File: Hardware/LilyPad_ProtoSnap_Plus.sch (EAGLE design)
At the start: 141 parts, among them J1 SEWTAP_LONG-2SIDE, J10 SEWTAP_LONG-2SIDE, J11 SEWTAP_LONG-2SIDE, J12 SEWTAP_LONG-2SIDE, J13 SEWTAP_LONG-2SIDE, J14 SEWTAP_LONG-2SIDE, J15 AMP FCI 10103594-0001LF, J2 SEWTAP_LONG-2SIDE, J3 SEWTAP_LONG-2SIDE, J4 SEWTAP_LONG-2SIDE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

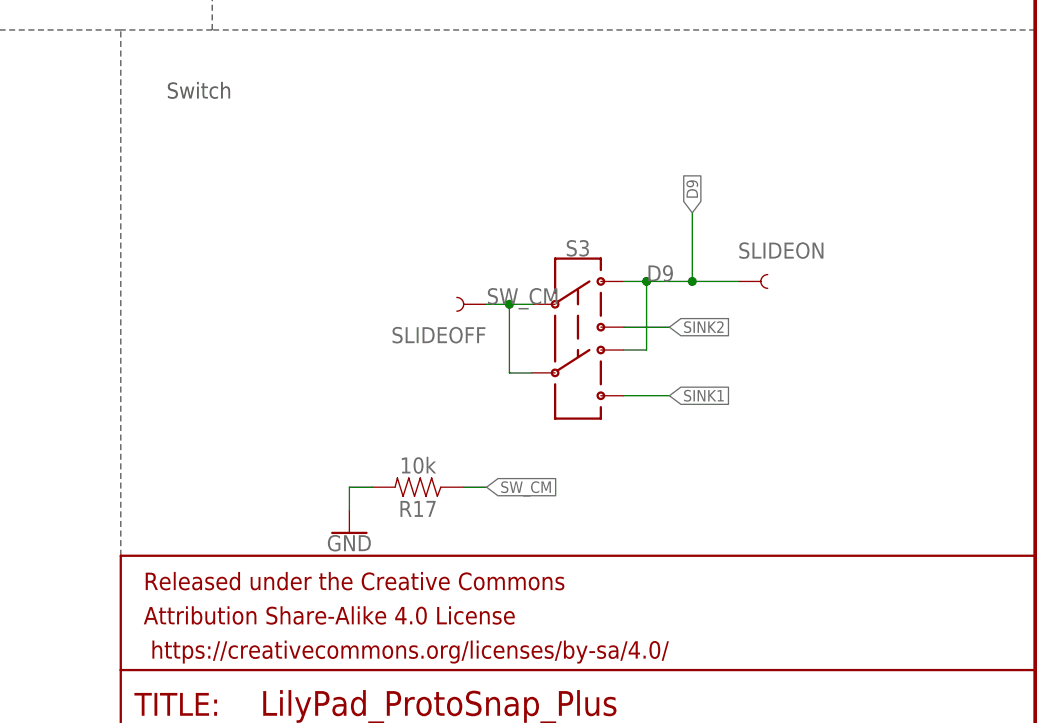
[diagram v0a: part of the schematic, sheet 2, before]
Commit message: Added changes from reds review
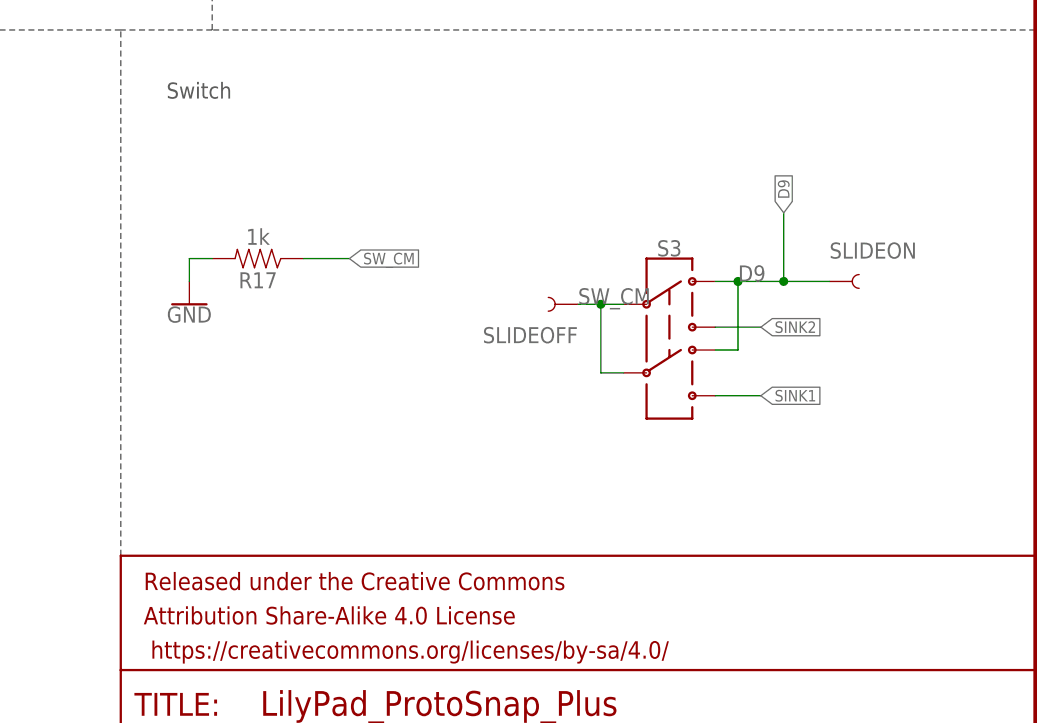
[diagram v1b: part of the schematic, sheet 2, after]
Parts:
- LED3: PROD_ID DIO-00819 -> (none)
- R17: value 10k -> 1k; device SparkFun-Resistors:10KOHM-0603-1/10W-1% -> SparkFun-Resistors:1KOHM-0603-1/10W-1%
- R6: value 330 -> 2.2k; device SparkFun-Resistors:330OHM-0603-1/10W-1% -> SparkFun-Resistors:2.2KOHM-0603-1/10W-1%; PROD_ID RES-00818 -> (none)
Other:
- note added: "Charge current factory set to 100mA I_CHG = 1000/R2"
- moved on the sheet: LED8, R17, R4, R5, S3, SLIDEOFF, SLIDEON

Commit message: Ran engineering checklist
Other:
- note added: "Supply 5.0V from USB, or 3.3-4.2V on battery connector."
- note removed: "v03"
- moved on the sheet: J16
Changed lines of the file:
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@@
 <setting verticaltext="up"/>
 </settings>
-<grid distance="0.1" unitdist="inch" unit="inch" style="lines" multiple="1" display="no" altdistance="0.05" altunitdist="inch" altunit="inch"/>
+<grid distance="0.1" unitdist="inch" unit="inch" style="lines" multiple="1" display="no" altdistance="0.01" altunitdist="inch" altunit="inch"/>
 <layers>
 <layer number="1" name="Top" color="4" fill="1" visible="no" active="no"/>
@@
 <text x="83.82" y="68.58" size="2.032" layer="97" font="vector">Charge current factory set to 100mA
 I_CHG = 1000/R2</text>
+<text x="5.08" y="5.08" size="2.032" layer="97" font="vector">Supply 5.0V from USB, or
+3.3-4.2V on battery connector.</text>
 </plain>
 <instances>
@@
 <attribute name="PROD_ID" x="139.7" y="93.98" size="1.27" layer="96" rot="R180" display="off"/>
 </instance>
-<instance part="LED2" gate="G$1" x="147.32" y="99.06" rot="R270">
+<instance part="LED2" gate="G$1" x="147.32" y="99.06" smashed="yes" rot="R270">
 <attribute name="PROD_ID" x="147.32" y="99.06" size="1.27" layer="96" rot="R270" display="off"/>
-</instance>
-<instance part="LED3" gate="G$1" x="154.94" y="93.98" rot="R270">
+<attribute name="NAME" x="142.748" y="105.791" size="1.778" layer="95" font="vector"/>
+<attribute name="VALUE" x="142.748" y="104.775" size="1.778" layer="96" font="vector" align="top-left"/>
+</instance>
+<instance part="LED3" gate="G$1" x="154.94" y="93.98" smashed="yes" rot="R270">
 <attribute name="PROD_ID" x="154.94" y="93.98" size="1.27" layer="96" rot="R270" display="off"/>
+<attribute name="NAME" x="150.368" y="89.789" size="1.778" layer="95" font="vector"/>
+<attribute name="VALUE" x="150.368" y="88.773" size="1.778" layer="96" font="vector" align="top-left"/>
 </instance>
 <instance part="LED4" gate="G$1" x="144.78" y="116.84" smashed="yes" rot="R90">
@@
 <attribute name="PROD_ID" x="101.6" y="45.72" size="1.778" layer="96" display="off"/>
 </instance>
-<instance part="GND11" gate="1" x="27.94" y="10.16"/>
-<instance part="U$4" gate="G$1" x="27.94" y="20.32"/>
+<instance part="GND11" gate="1" x="27.94" y="17.78"/>
+<instance part="U$4" gate="G$1" x="27.94" y="27.94"/>
 <instance part="GND12" gate="1" x="165.1" y="109.22"/>
 <instance part="U5" gate="G1" x="63.5" y="124.46"/>
@@
 <attribute name="NAME" x="33.02" y="43.18" size="1.778" layer="95" font="vector" rot="R180"/>
 </instance>
-<instance part="J16" gate="G$1" x="20.32" y="15.24" rot="R90"/>
+<instance part="J16" gate="G$1" x="20.32" y="22.86" rot="R90"/>
 <instance part="GND10" gate="1" x="10.16" y="106.68"/>
 <instance part="SUPPLY1" gate="G$2" x="109.22" y="50.8"/>
@@
 </segment>
 <segment>
-<wire x1="25.4" y1="17.78" x2="27.94" y2="17.78" width="0.1524" layer="91"/>
-<wire x1="27.94" y1="17.78" x2="27.94" y2="20.32" width="0.1524" layer="91"/>
+<wire x1="25.4" y1="25.4" x2="27.94" y2="25.4" width="0.1524" layer="91"/>
+<wire x1="27.94" y1="25.4" x2="27.94" y2="27.94" width="0.1524" layer="91"/>
 <pinref part="U$4" gate="G$1" pin="V_BATT"/>
 <pinref part="J16" gate="G$1" pin="+"/>
@@
 <segment>
 <pinref part="GND11" gate="1" pin="GND"/>
-<wire x1="25.4" y1="15.24" x2="27.94" y2="15.24" width="0.1524" layer="91"/>
-<wire x1="27.94" y1="15.24" x2="27.94" y2="12.7" width="0.1524" layer="91"/>
+<wire x1="25.4" y1="22.86" x2="27.94" y2="22.86" width="0.1524" layer="91"/>
+<wire x1="27.94" y1="22.86" x2="27.94" y2="20.32" width="0.1524" layer="91"/>
 <pinref part="J16" gate="G$1" pin="-"/>
 </segment>
@@
 <text x="53.34" y="86.36" size="1.778" layer="97">Buzzer</text>
 <text x="171.45" y="11.43" size="2.54" layer="94">Marshall Taylor</text>
-<text x="238.252" y="7.112" size="2.54" layer="94">v03</text>
+<text x="238.252" y="7.112" size="2.54" layer="94">v10</text>
 <text x="60.96" y="25.4" size="1.778" layer="97">Un-used
 sew taps</text>

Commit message: Updated reds QC check
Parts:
- D10: device newLilypadParts:SUNLEDSMD1 -> SparkFun-LED:SUNLEDSMD1
- U5: value ATMEGA32U4_NOARDQFN3 -> 32U4; device newLilypadParts:ATMEGA32U4_NOARDQFN3 -> SparkFun-IC-Microcontroller:ATMEGA32U4_NOARDQFN3
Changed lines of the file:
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@@
 <part name="U$4" library="SparkFun-PowerSymbols" deviceset="V_BATT" device=""/>
 <part name="GND12" library="SparkFun-PowerSymbols" deviceset="GND" device=""/>
-<part name="U5" library="newLilypadParts" deviceset="ATMEGA32U4_NOARD" device="QFN3" value="ATMEGA32U4_NOARDQFN3"/>
+<part name="U5" library="SparkFun-IC-Microcontroller" deviceset="ATMEGA32U4_NOARD" device="QFN3" value="32U4"/>
 <part name="J1" library="LilyPad-Wearables" deviceset="SEWTAP" device="_LONG-2SIDE" value="SEWTAP_LONG-2SIDE"/>
 <part name="J2" library="LilyPad-Wearables" deviceset="SEWTAP" device="_LONG-2SIDE" value="SEWTAP_LONG-2SIDE"/>
@@
 <part name="LOGO5" library="SparkFun-Aesthetics" deviceset="OSHW-LOGO" device="S"/>
 <part name="LOGO6" library="SparkFun-Aesthetics" deviceset="OSHW-LOGO" device="S"/>
-<part name="D10" library="newLilypadParts" deviceset="SUNLED" device="SMD1" value="XZM2CRKM2DGFBB45SCCB"/>
+<part name="D10" library="SparkFun-LED" deviceset="SUNLED" device="SMD1" value="XZM2CRKM2DGFBB45SCCB"/>
 <part name="TP5" library="SparkFun-Connectors" deviceset="TEST-POINT" device="3"/>
 <part name="TP6" library="SparkFun-Connectors" deviceset="TEST-POINT" device="3"/>

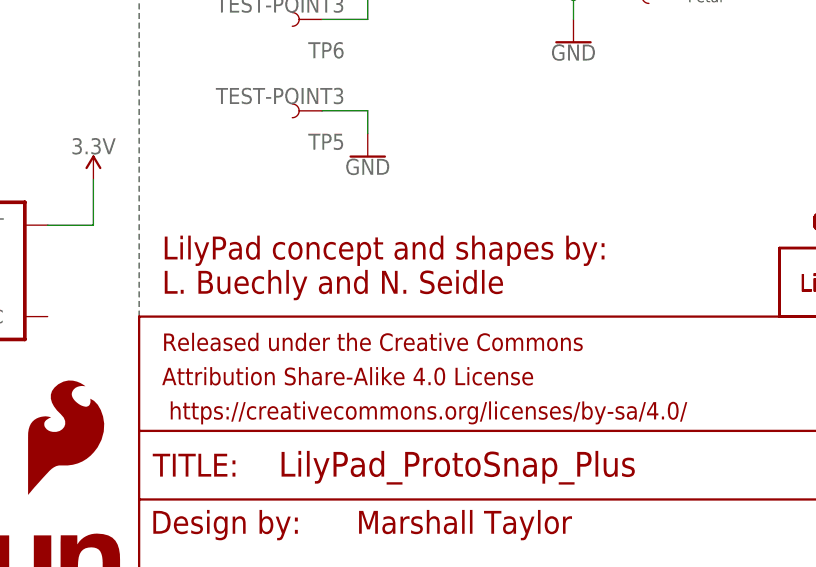
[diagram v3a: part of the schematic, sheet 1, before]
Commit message: Fixed spelling error
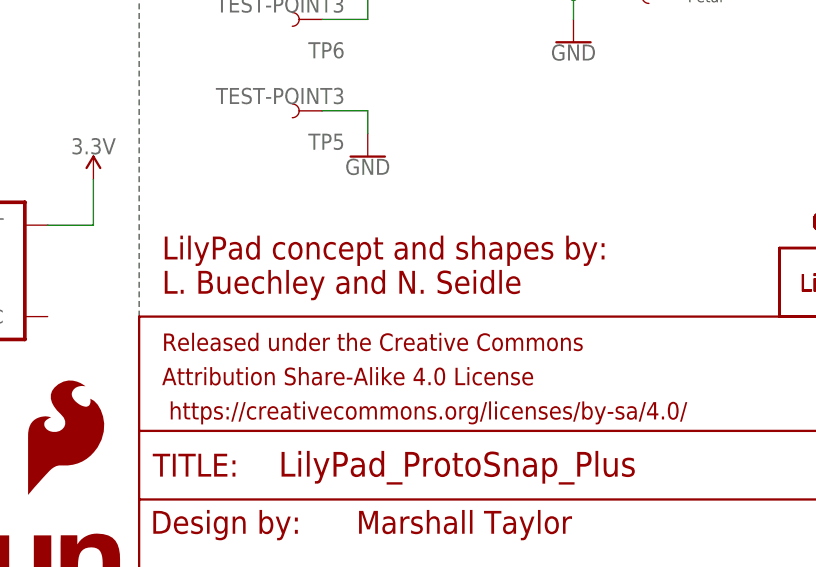
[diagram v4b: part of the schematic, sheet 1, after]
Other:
- note added: "LilyPad concept and shapes by: L. Buechley and N. Seidle"
- note removed: "LilyPad concept and shapes by: L. Buechly and N. Seidle"
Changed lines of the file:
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@@
 <text x="238.252" y="7.112" size="2.54" layer="94">v10</text>
 <text x="149.86" y="38.1" size="2.54" layer="94">LilyPad concept and shapes by:
-L. Buechly and N. Seidle</text>
+L. Buechley and N. Seidle</text>
 <wire x1="223.52" y1="182.88" x2="246.38" y2="182.88" width="0.1524" layer="97" style="shortdash"/>
 <wire x1="246.38" y1="182.88" x2="246.38" y2="154.94" width="0.1524" layer="97" style="shortdash"/>

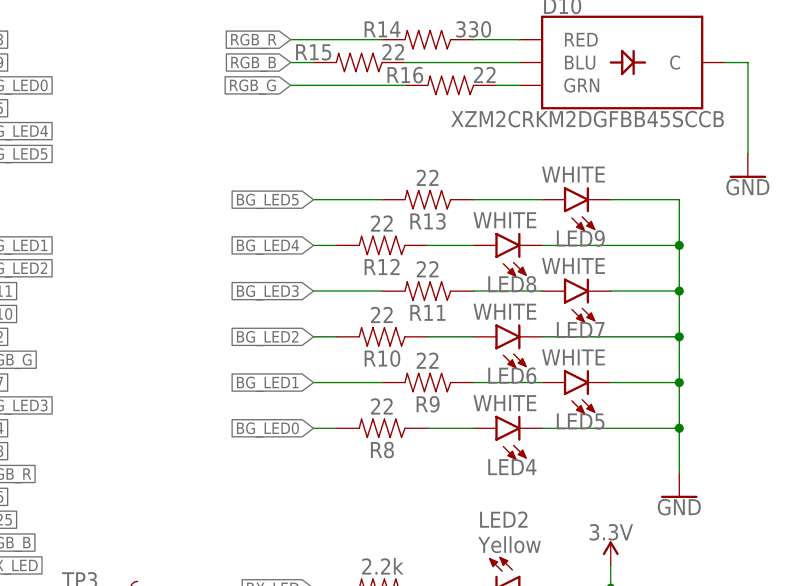
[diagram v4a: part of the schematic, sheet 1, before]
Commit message: Changed bargraph resistors to 470 ohm
To reduce brightness of white LED bargraph, changed R8-R13 inclusive
from 22 ohm to 470 ohm 0402 RES-13829 (new part)
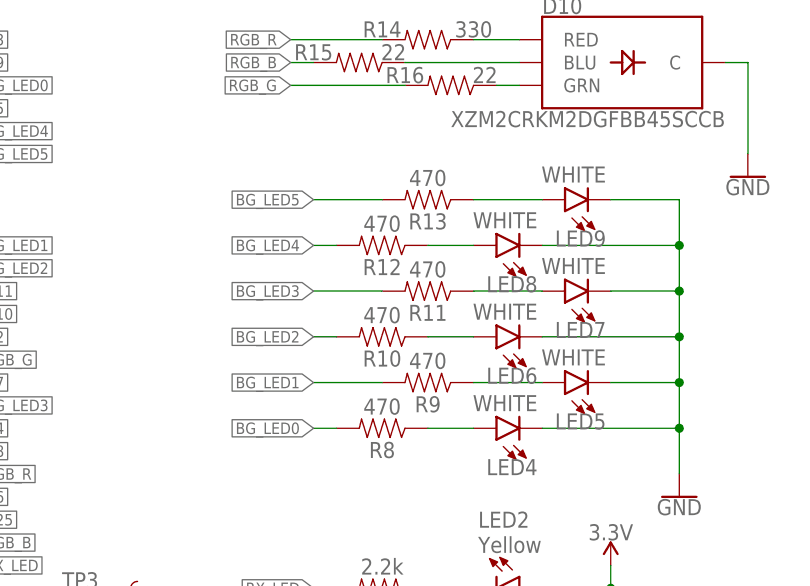
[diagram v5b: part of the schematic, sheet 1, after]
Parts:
- R10, R11, R12, R13, R8, R9: value 22 -> 470; device SparkFun-Resistors:22OHM-0402-1/10W-1% -> SparkFun-Resistors:470OHM-0402-1/16W-5%
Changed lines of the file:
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@@
 <?xml version="1.0" encoding="utf-8"?>
 <!DOCTYPE eagle SYSTEM "eagle.dtd">
-<eagle version="7.7.0">
+<eagle version="7.4.0">
 <drawing>
 <settings>
@@
 <part name="LED3" library="SparkFun-LED" deviceset="LED-GREEN" device="0603" value="GREEN"/>
 <part name="LED4" library="SparkFun-LED" deviceset="LED-WHITE" device="0603" value="WHITE"/>
-<part name="R8" library="SparkFun-Resistors" deviceset="22OHM" device="-0402-1/10W-1%" value="22"/>
+<part name="R8" library="SparkFun-Resistors" deviceset="470OHM" device="-0402-1/16W-5%" value="470"/>
 <part name="P+3" library="SparkFun-PowerSymbols" deviceset="3.3V" device=""/>
 <part name="C2" library="SparkFun-Capacitors" deviceset="0.1UF" device="-0402-16V-10%" value="0.1uF"/>
@@
 <part name="LED6" library="SparkFun-LED" deviceset="LED-WHITE" device="0603" value="WHITE"/>
 <part name="LED7" library="SparkFun-LED" deviceset="LED-WHITE" device="0603" value="WHITE"/>
-<part name="R9" library="SparkFun-Resistors" deviceset="22OHM" device="-0402-1/10W-1%" value="22"/>
-<part name="R10" library="SparkFun-Resistors" deviceset="22OHM" device="-0402-1/10W-1%" value="22"/>
-<part name="R11" library="SparkFun-Resistors" deviceset="22OHM" device="-0402-1/10W-1%" value="22"/>
+<part name="R9" library="SparkFun-Resistors" deviceset="470OHM" device="-0402-1/16W-5%" value="470"/>
+<part name="R10" library="SparkFun-Resistors" deviceset="470OHM" device="-0402-1/16W-5%" value="470"/>
+<part name="R11" library="SparkFun-Resistors" deviceset="470OHM" device="-0402-1/16W-5%" value="470"/>
 <part name="GND13" library="SparkFun-PowerSymbols" deviceset="GND" device=""/>
 <part name="P+5" library="SparkFun-PowerSymbols" deviceset="3.3V" device=""/>
 <part name="LED8" library="SparkFun-LED" deviceset="LED-WHITE" device="0603" value="WHITE"/>
-<part name="R12" library="SparkFun-Resistors" deviceset="22OHM" device="-0402-1/10W-1%" value="22"/>
+<part name="R12" library="SparkFun-Resistors" deviceset="470OHM" device="-0402-1/16W-5%" value="470"/>
 <part name="LED9" library="SparkFun-LED" deviceset="LED-WHITE" device="0603" value="WHITE"/>
-<part name="R13" library="SparkFun-Resistors" deviceset="22OHM" device="-0402-1/10W-1%" value="22"/>
+<part name="R13" library="SparkFun-Resistors" deviceset="470OHM" device="-0402-1/16W-5%" value="470"/>
 <part name="J15" library="SparkFun-Connectors" deviceset="USB_MICRO-B" device="_HALF_PTH" value="AMP FCI 10103594-0001LF"/>
 <part name="J16" library="SparkFun-Connectors" deviceset="JST_2MM_MALE" device=""/>
